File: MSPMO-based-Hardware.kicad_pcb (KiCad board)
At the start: 2 copper layers, 53 x 28 mm, 36 parts, among them J1 Conn_ARM_SWD_TagConnect_TC2030, J2 USB_C_Receptacle_USB2.0_16P, U1 SPX3819M5-L-3-3, U3 MSPMOG3507SPTR, U4 CH340E, U5 LIS2DH, X1 8MHz

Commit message: chore(hardware): reposition components and add design to PCB layout
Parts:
- moved C2 7.83 mm to (66.7, 91.8), turned to -90 degrees
- moved C1 1.31 mm to (73.5, 91.7), turned to 90 degrees
- moved R1 0.18 mm to (62.0, 101.6)
- moved R3 0.07 mm to (62.9, 96.1)

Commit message: feat(hardware): add L2 GND ground plane zone to PCB layout
- Added new bottom copper layer GND polygon zone (L2_GND) for improved ground connectivity
- Updated zone connection settings for GND pin to optimize electrical performance
- These changes enhance the PCB's grounding design and signal integrity
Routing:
- added copper zone on B.Cu, net GND
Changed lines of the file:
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@@
 			(pinfunction "1")
 			(pintype "input")
-			(zone_connect 2)
+			(zone_connect 1)
 		)
 		(pad "1" thru_hole circle
@@
 			)
 		)
+	)
+	(zone
+		(net 2)
+		(net_name "GND")
+		(layer "B.Cu")
+		(name "L2_GND")
+		(hatch edge 0.5)
+		(connect_pads
+			(clearance 0.4)
+		)
+		(min_thickness 0.2)
+		(filled_areas_thickness no)
+		(fill yes
+			(thermal_gap 0.3)
+			(thermal_bridge_width 0.3)
+			(smoothing fillet)
+			(radius 4)
+		)
+		(polygon
+			(pts
+				(xy 52 85) (xy 106 85) (xy 106 114) (xy 52 114)
+			)
+		)

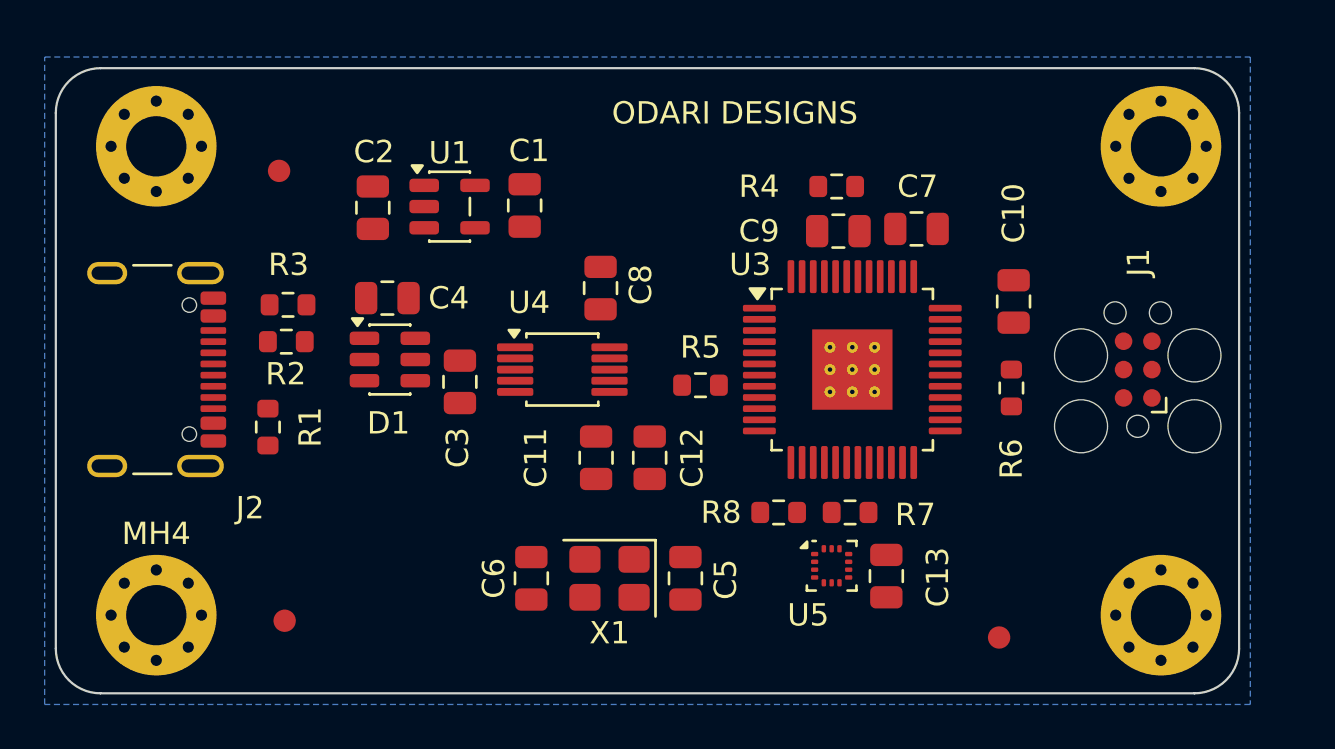
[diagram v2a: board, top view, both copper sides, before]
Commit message: feat(hardware): add routing vias and reposition PCB components
Add approximately 50 new vias with copper trace segments to improve PCB routing connectivity. Reposition multiple components including capacitors (C2-C13), resistors (R1-R5, R8), and IC (U1) to optimize board layout. Update component reference designator positions and rotation angles for better assembly.
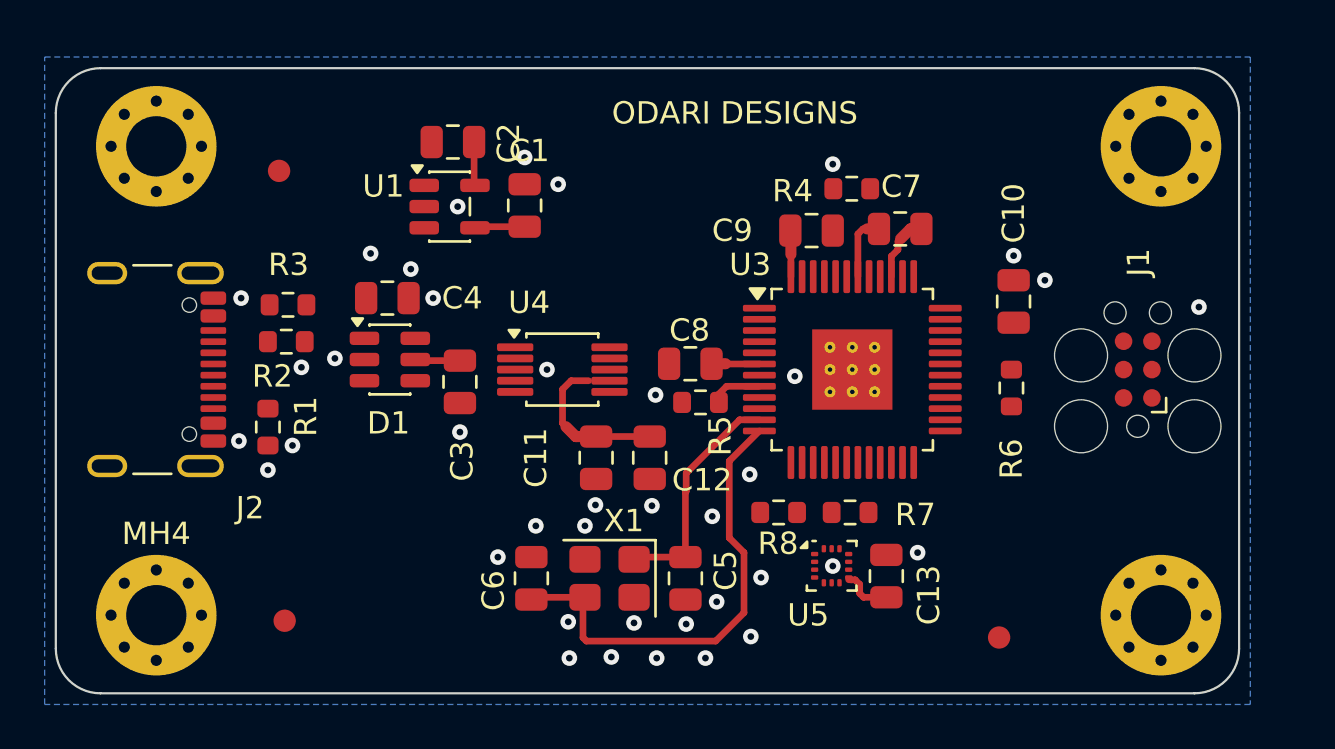
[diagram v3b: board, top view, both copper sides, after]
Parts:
- moved C8 5.26 mm to (80.9, 98.7), turned to 180 degrees
- moved C2 4.64 mm to (70.3, 88.8), turned to 180 degrees
- moved C9 1.20 mm to (86.3, 92.8)
- moved R5 0.77 mm to (81.4, 100.5)
- moved C7 0.73 mm to (90.3, 92.7)
- moved R4 0.68 mm to (88.2, 90.9)
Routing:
- net /HFXOUT: track 0.00 -> 21.1 mm
- net +3.3V: track 0.00 -> 13.4 mm
- net /HFXIN: track 0.00 -> 10.4 mm
- net /VREF-: track 0.00 -> 2.98 mm
- net /VREF+: track 0.00 -> 2.95 mm
- net /ROSC: track 0.00 -> 2.33 mm
- net Net-(U1-BP): track 0.00 -> 2.25 mm
- net +VBUS: track 0.00 -> 2.02 mm
- net +1V35: track 0.00 -> 1.85 mm
- net GND: vias 0 -> 30
- net (no net): vias 0 -> 9

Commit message: fix(hardware): remap USB differential signals to UART flow control pins
Renamed hierarchical labels in CH340E schematic to properly map USB D+/D- signals to UART0 RTS/CTS pins, correcting the signal routing configuration.
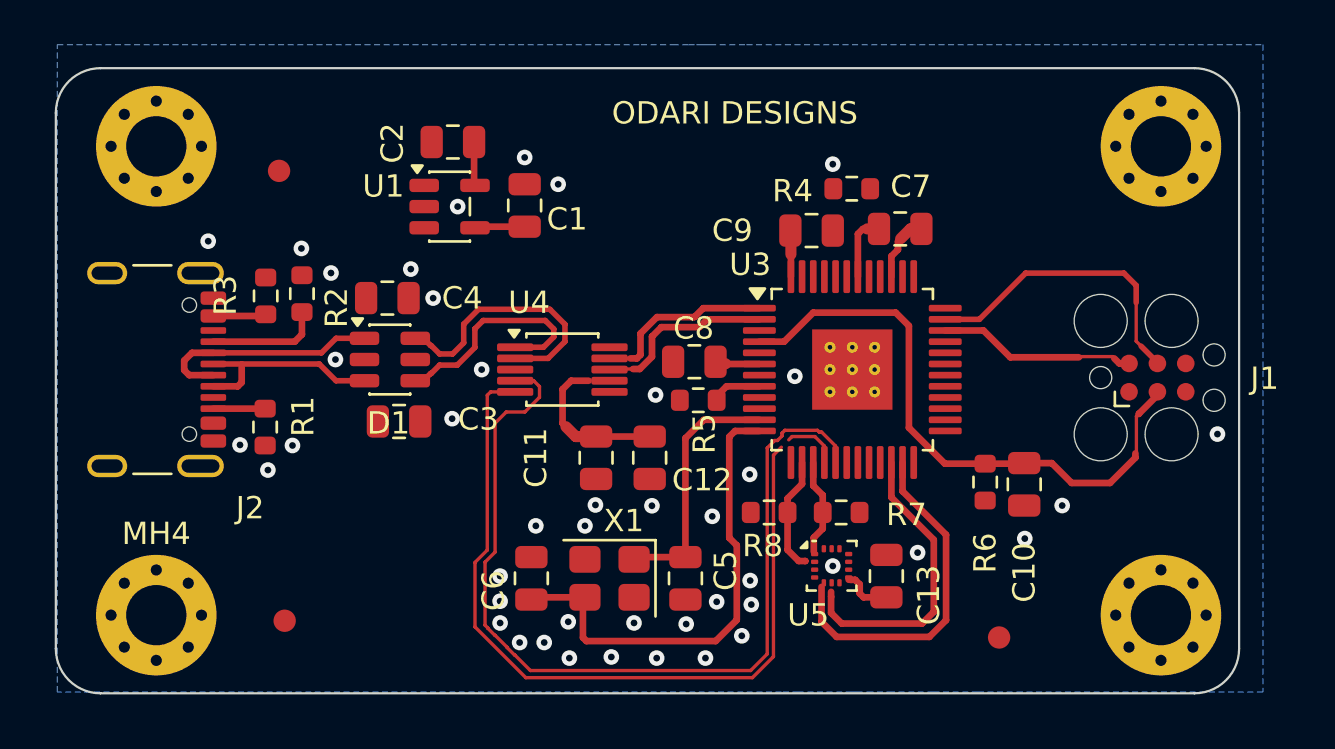
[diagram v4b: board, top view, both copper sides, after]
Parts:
- moved C10 8.20 mm to (95.9, 104.1), turned to -90 degrees
- moved R6 4.38 mm to (94.1, 104.0)
- moved C3 3.25 mm to (67.9, 101.3), turned to 0 degrees
- moved R2 2.26 mm to (63.5, 95.6), turned to 90 degrees
- moved R3 1.08 mm to (61.9, 95.7), turned to 90 degrees
- moved J1 0.95 mm to (101.8, 99.4), turned to 0 degrees
- moved R8 0.42 mm to (84.5, 105.4)
- moved R7 0.40 mm to (87.7, 105.4)
- moved C8 0.20 mm to (81.1, 98.7)
- moved R5 0.14 mm to (81.3, 100.4)
- moved R1 0.12 mm to (61.9, 101.6)
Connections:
- D1 pad 1: Net-(D1-I/O1-Pad1) -> /USBCD-
- D1 pad 3: Net-(D1-I/O2-Pad3) -> /USBCD+
- J2 pad A5: /USBCD- -> Net-(J2-CC1)
- J2 pad A6: Net-(D1-I/O2-Pad3) -> /USBCD+
- J2 pad A7: Net-(D1-I/O1-Pad1) -> /USBCD-
- J2 pad B5: /USBCD+ -> Net-(J2-CC2)
- J2 pad B6: Net-(D1-I/O2-Pad3) -> /USBCD+
- J2 pad B7: Net-(D1-I/O1-Pad1) -> /USBCD-
- R1 pad 1: /USBCD+ -> Net-(J2-CC2)
- R2 pad 1: /USBCD- -> Net-(J2-CC1)
- U5 pad 5: /INT2 -> /INT1
- U5 pad 6: /INT1 -> unconnected-(U5-INT1-Pad6)
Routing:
- net /UART0CTS: track 0.00 -> 40.9 mm
- net /UART0RTS: track 0.00 -> 38.7 mm
- net /NRST: track 0.00 -> 27.0 mm
- net /INT1: track 0.00 -> 15.6 mm
- net /SWCLK: track 0.00 -> 13.5 mm
- net /INT2: track 0.00 -> 13.4 mm
- net /USBD-: track 0.00 -> 11.9 mm
- net /USBCD-: track 0.00 -> 10.3 mm
- net /USBD+: track 0.00 -> 10.2 mm
- net /USBCD+: track 0.00 -> 9.10 mm
- net /SWDIO: track 0.00 -> 8.84 mm
- net /UART0RX: track 0.00 -> 8.21 mm
- net /UART0TX: track 0.00 -> 8.20 mm
- net /I2CSDA: track 0.00 -> 5.19 mm
- net Net-(J2-CC1): track 0.00 -> 5.10 mm
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
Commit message: fix(hardware): reposition components and optimize PCB routing
- Relocated J1 Tag-Connect header and J2 USB-C connector to resolve routing conflicts
- Adjusted resistor and capacitor positions (R2, R3, R6, R8, C3, C6, C7, C9, C10, C13)
- Realigned U5 LIS2DH12 accelerometer for better placement
- Added new vias and net segments to improve signal routing
- Expanded GND copper pours on both F.Cu and B.Cu layers
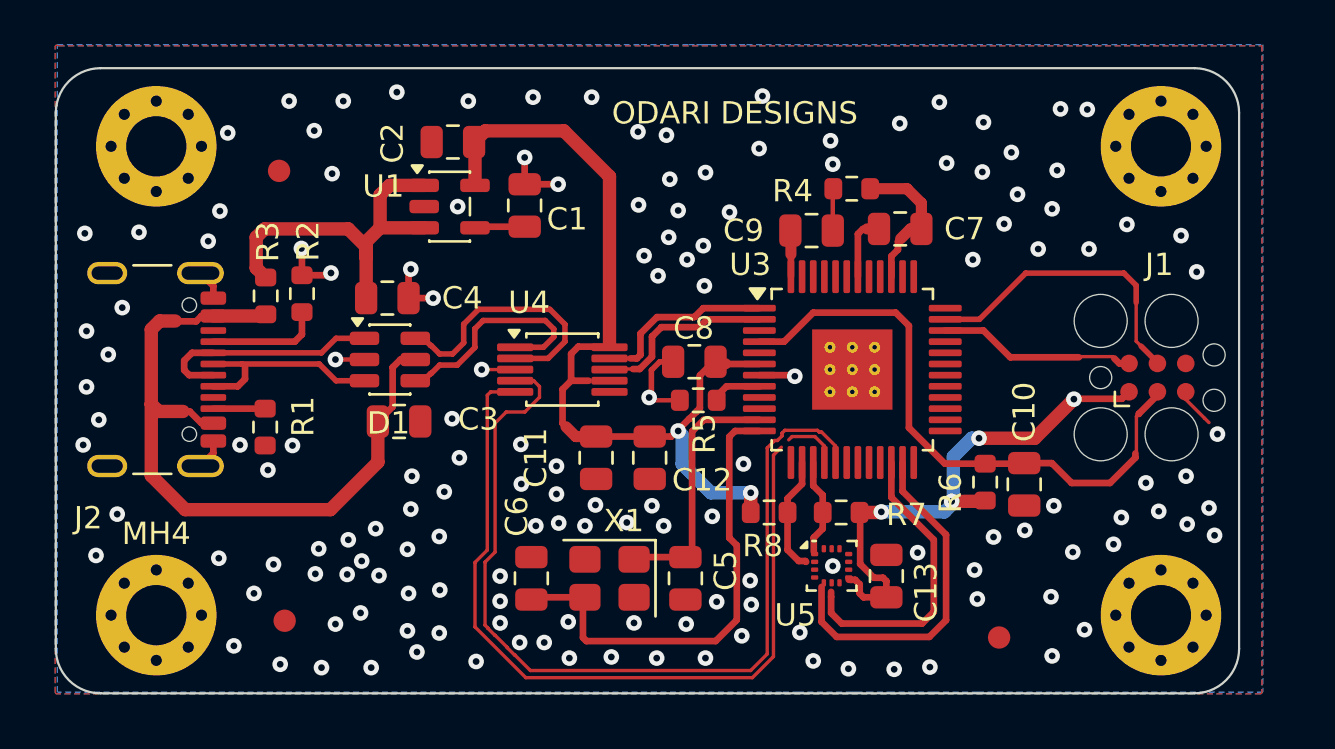
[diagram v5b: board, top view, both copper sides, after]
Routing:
- net +3.3V: track 13.4 -> 63.6 mm, vias 0 -> 6
- net +VBUS: track 2.45 -> 32.5 mm
- net GND: track 0.00 -> 22.9 mm, vias 34 -> 143
- net +5V: track 0.00 -> 16.9 mm
- net /VREF-: track 2.98 -> 6.70 mm
- added copper zone on F.Cu, net GND
